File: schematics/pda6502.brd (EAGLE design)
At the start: 100 x 80 mm, 35 parts, among them IC1 74HC00D, IC2 74HC138D, IC3 DS1813-SMD, J1 CON_HEADER_2X07-PTH, U1 W65C02S, U2 W65C22S, U3 28C256, U4 UM61256AK-12

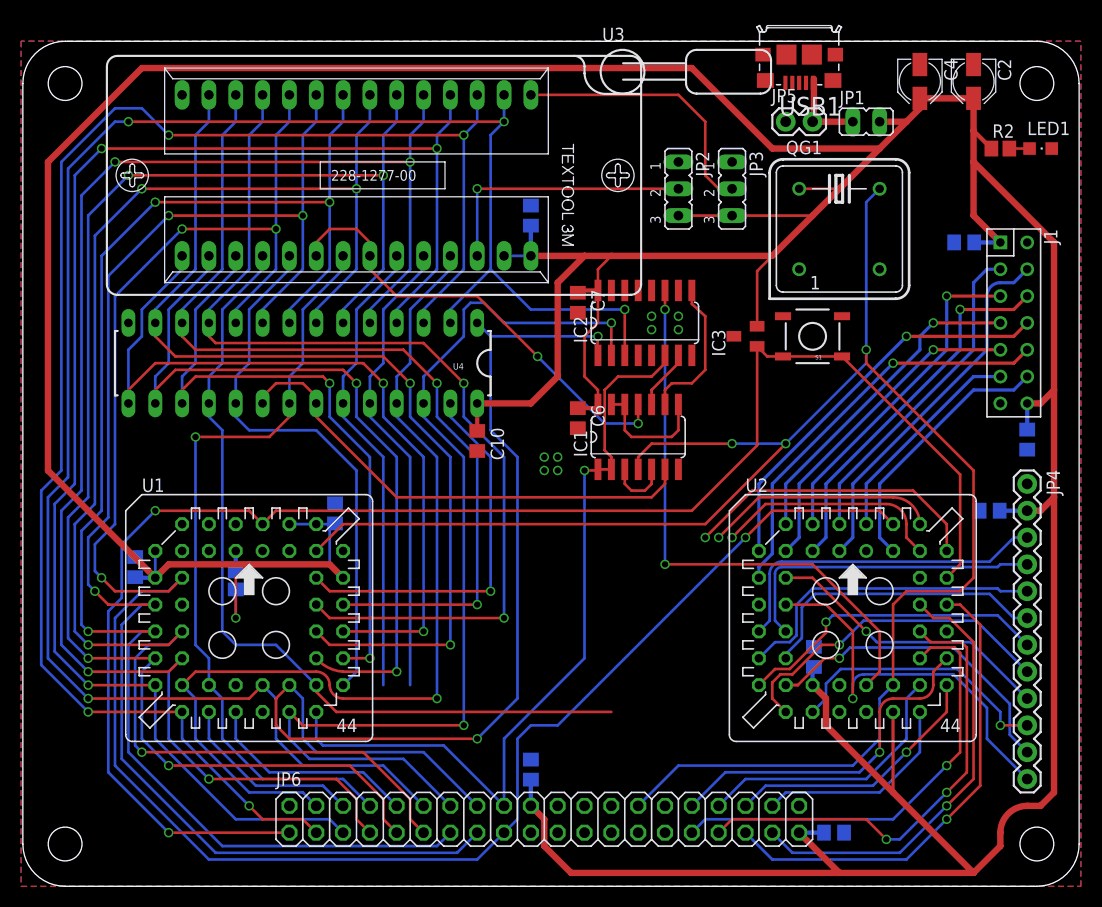
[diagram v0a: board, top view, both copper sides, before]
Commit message: board: 6502 bumped 50 mils right; left-side traces straightened.
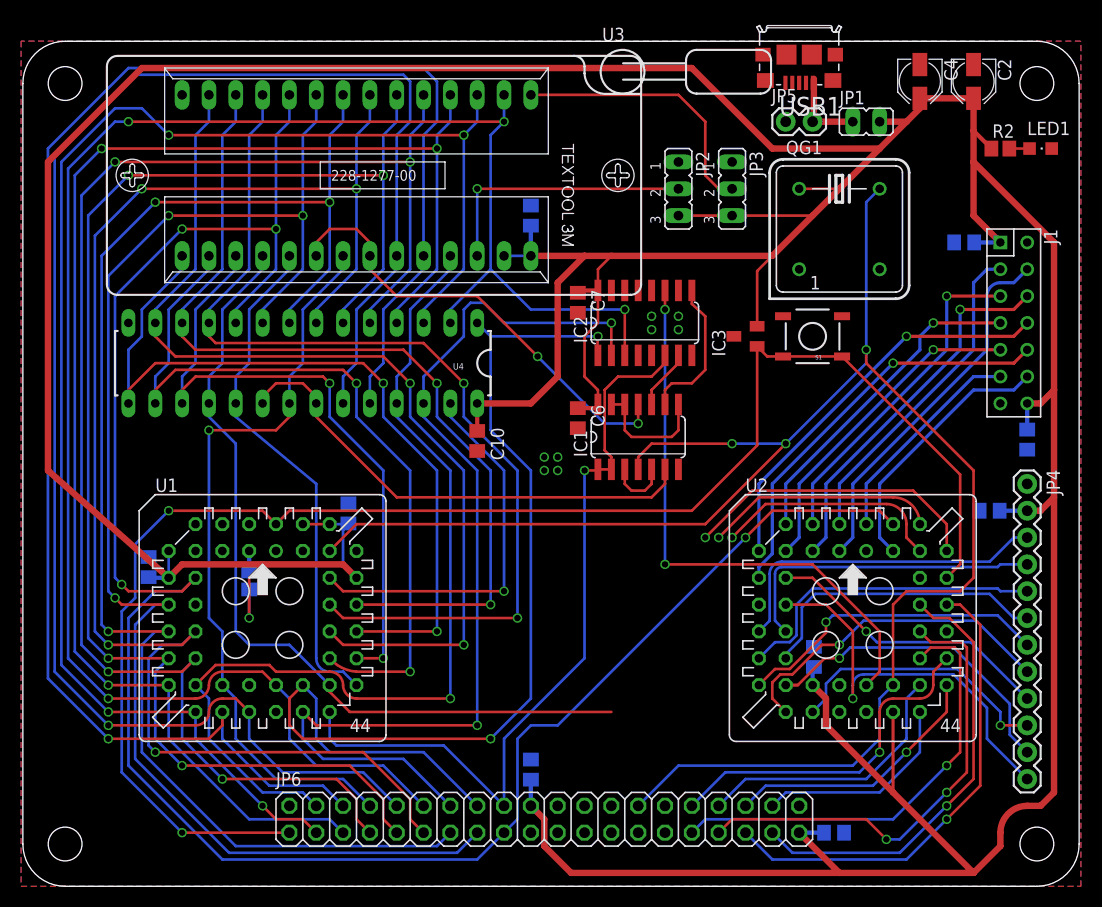
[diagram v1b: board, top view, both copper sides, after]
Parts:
- moved C1 1.27 mm to (12.1, 30.2)
- moved C3 1.27 mm to (31.0, 35.3)
- moved R1 1.27 mm to (21.6, 29.0)
- moved U1 1.27 mm to (22.9, 26.7)
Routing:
- net ADDR9: track 62.2 -> 161.1 mm, vias 0 -> 1
- net ADDR11: track 64.7 -> 160.3 mm, vias 0 -> 1
- net DATA7: track 71.6 -> 68.5 mm
- net ADDR7: track 147.5 -> 144.8 mm
- net ADDR5: track 144.5 -> 141.8 mm
- net ADDR4: track 140.1 -> 137.4 mm
- net ADDR3: track 173.9 -> 171.2 mm
- net ADDR2: track 159.9 -> 157.3 mm
- net ADDR6: track 142.3 -> 139.6 mm
- net RESB: track 150.6 -> 148.1 mm
- net ADDR1: track 158.1 -> 155.8 mm
- net ADDR0: track 195.9 -> 193.5 mm
- net ADDR10: track 73.3 -> 71.1 mm
- net ADDR12: track 177.2 -> 175.6 mm
- net PHI2: track 165.3 -> 164.1 mm
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
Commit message: board: 6502 bumped further right; opens gap for ground pour.
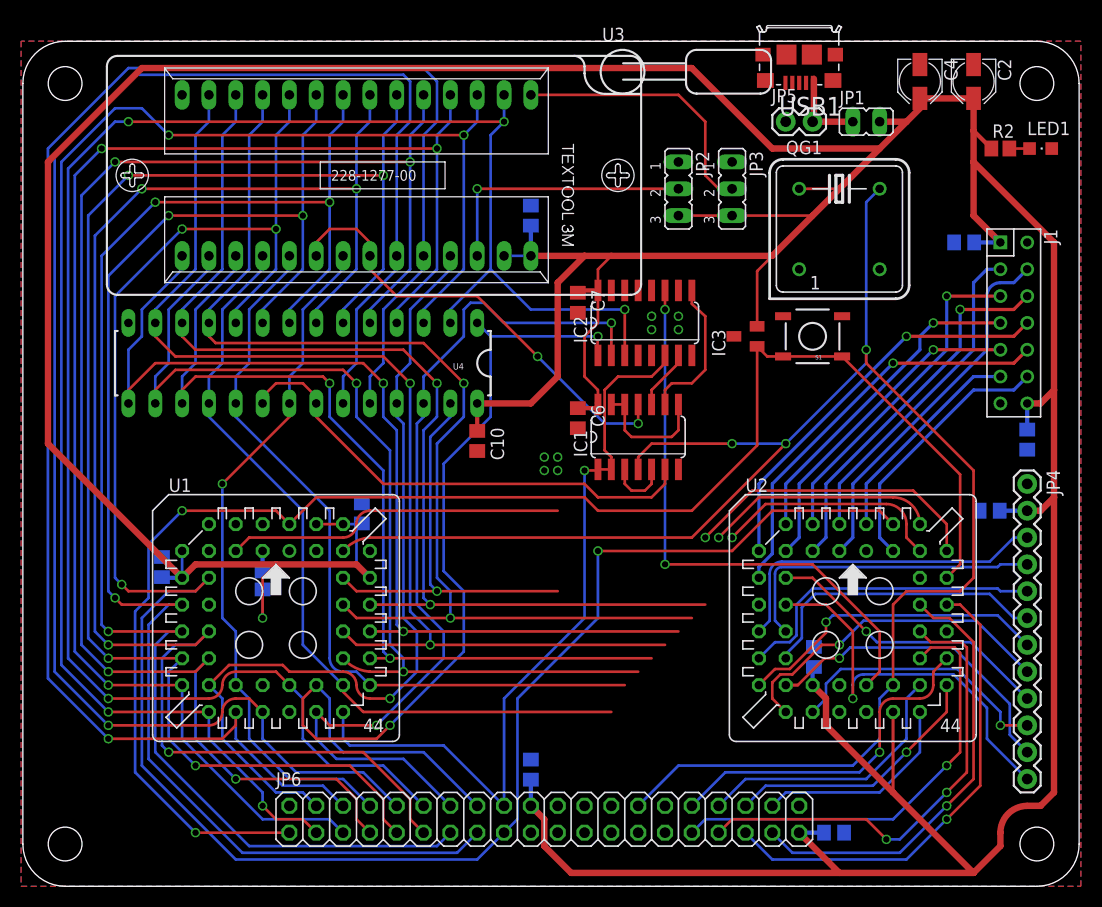
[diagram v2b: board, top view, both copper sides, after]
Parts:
- moved C3 1.27 mm to (32.3, 35.3)
- moved C1 1.27 mm to (13.3, 30.2)
- moved R1 1.27 mm to (22.9, 29.0)
- moved U1 1.27 mm to (24.1, 26.7)
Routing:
- net IRQB: track 0.00 -> 32.1 mm
- net DATA5: track 88.8 -> 113.2 mm
- net DATA7: track 68.5 -> 92.8 mm
- net DATA3: track 118.9 -> 139.2 mm
- net DATA4: track 107.9 -> 128.0 mm
- net DATA1: track 132.1 -> 149.8 mm
- net DATA2: track 135.4 -> 151.8 mm
- net DATA0: track 135.8 -> 150.5 mm
- net ADDR14: track 102.7 -> 92.2 mm
- net ADDR13: track 97.3 -> 87.1 mm
- net ADDR8: track 90.7 -> 82.2 mm
- net ADDR0: track 193.5 -> 199.5 mm
- net ADDR10: track 71.1 -> 65.6 mm
- net DATA6: track 103.1 -> 100.1 mm
- net RWB: track 36.9 -> 39.7 mm
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
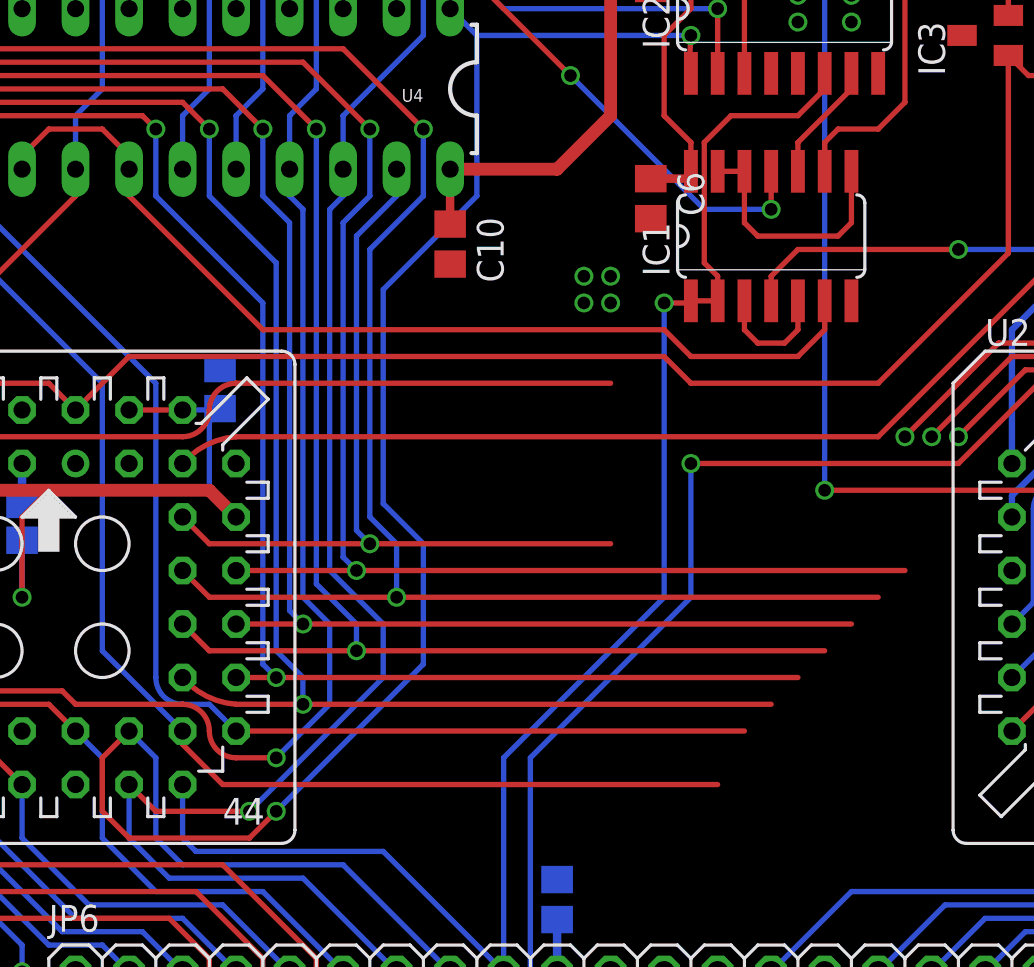
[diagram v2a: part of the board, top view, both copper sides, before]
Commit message: board: clearance to right of 6502 for ground pour.
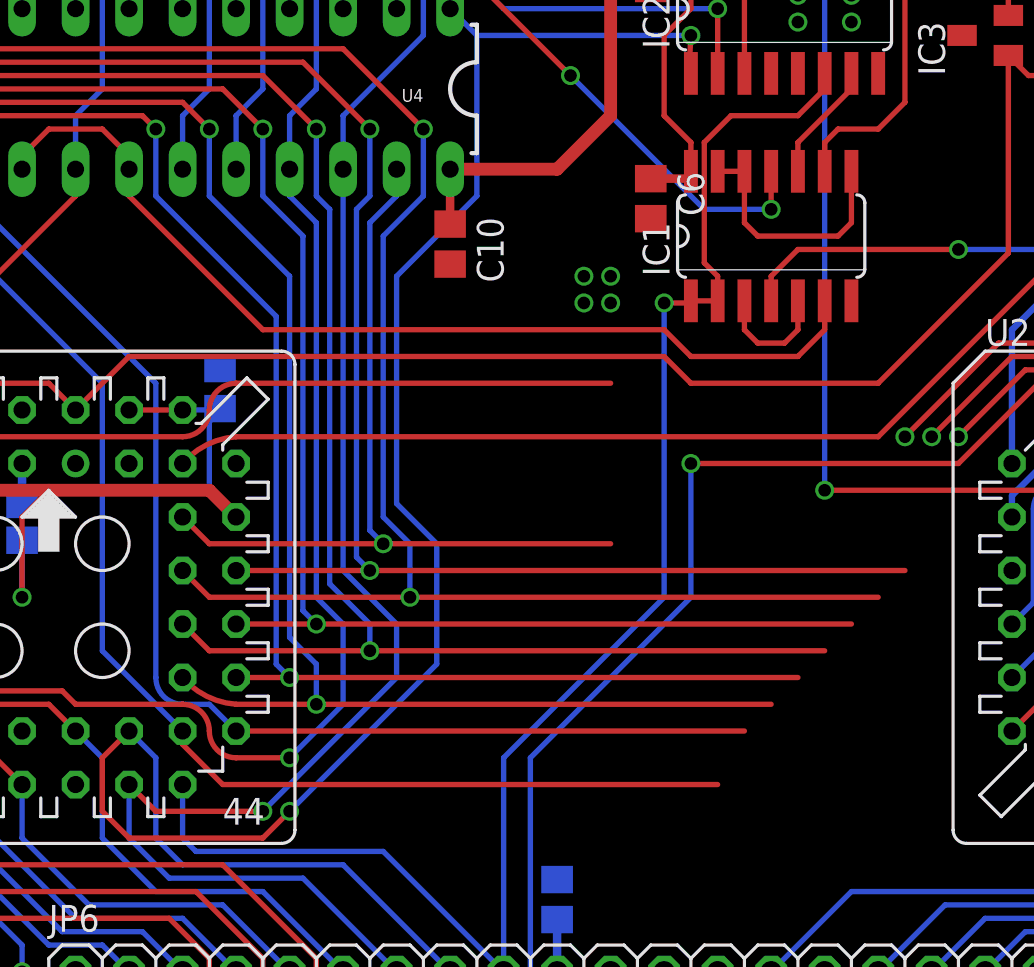
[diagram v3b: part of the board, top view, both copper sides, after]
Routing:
- net ADDR8: track 82.2 -> 83.1 mm

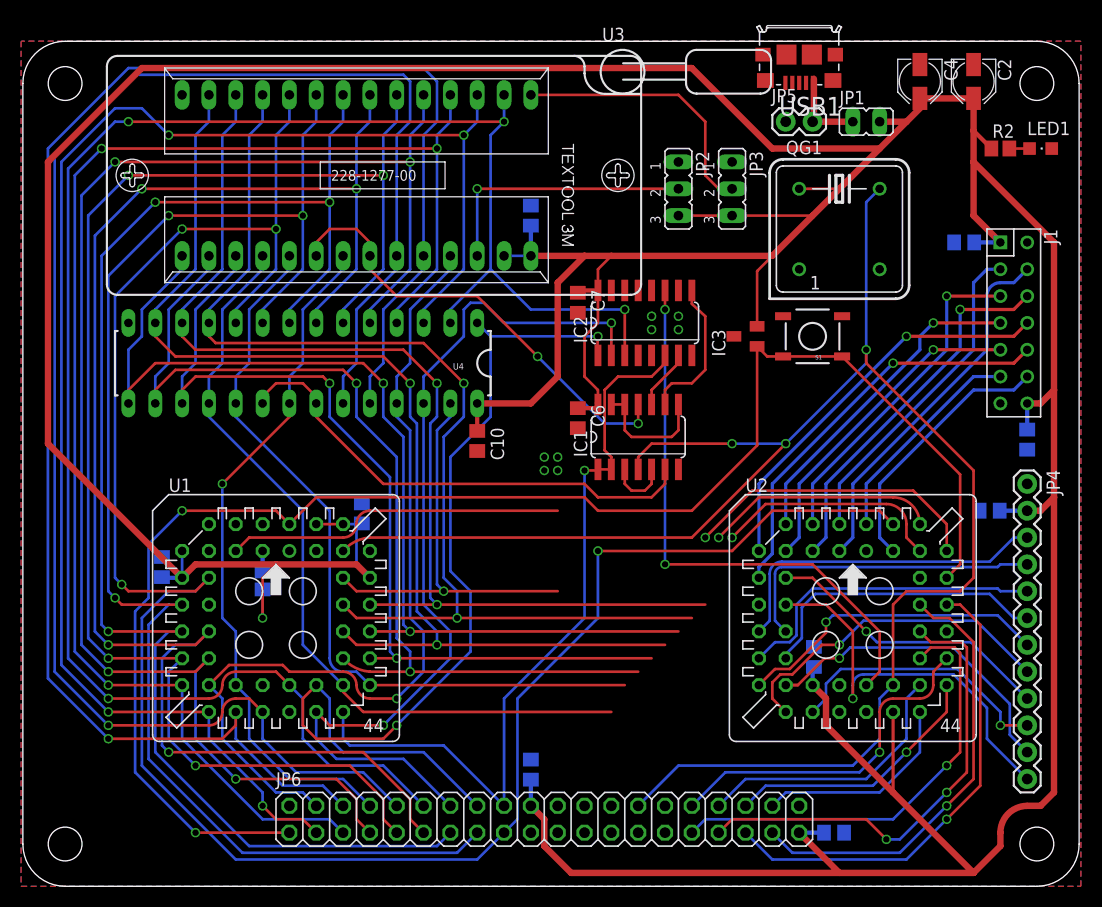
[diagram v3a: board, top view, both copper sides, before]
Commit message: board: 6 airwires; likely all GND plane issues.
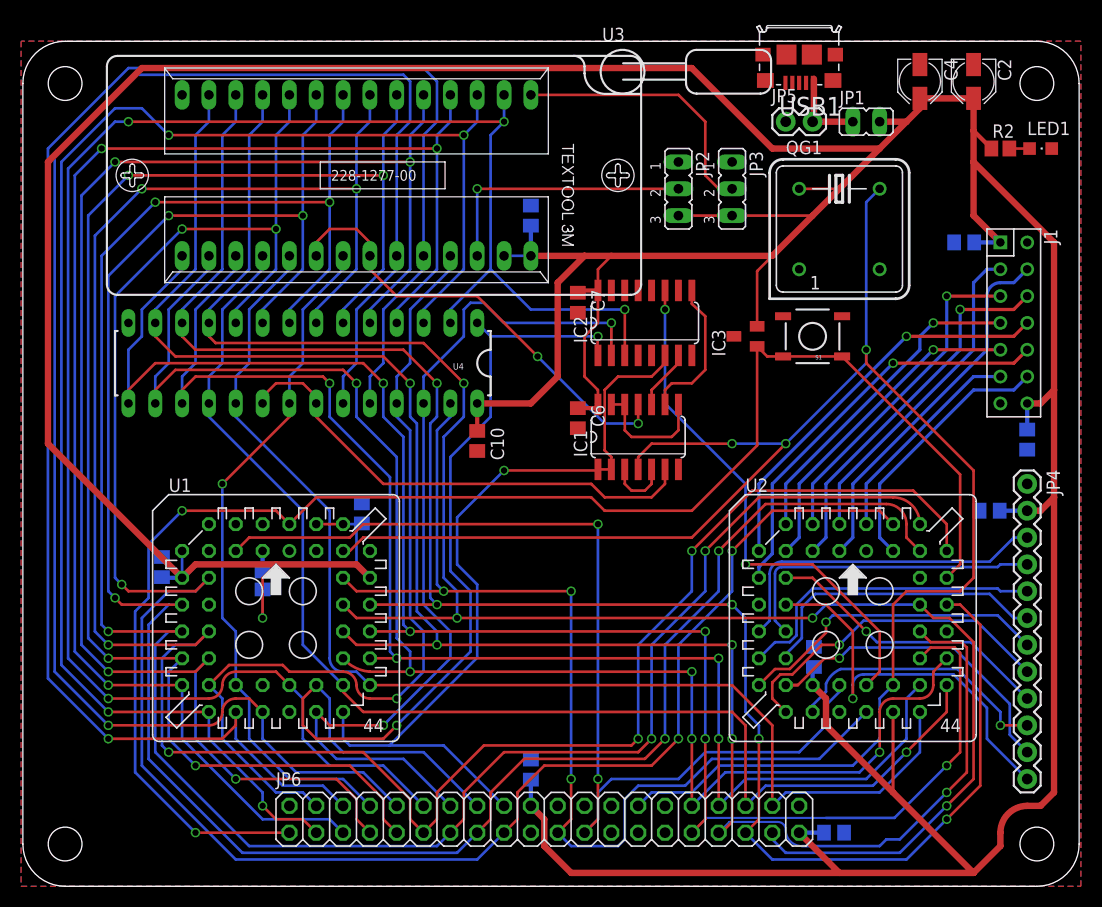
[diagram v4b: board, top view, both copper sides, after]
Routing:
- net IRQB: track 32.1 -> 98.0 mm, vias 0 -> 2
- net RWB: track 39.4 -> 101.3 mm, vias 1 -> 3
- net ADDR3: track 171.2 -> 218.4 mm, vias 5 -> 6
- net ADDR2: track 157.3 -> 203.2 mm, vias 4 -> 5
- net ADDR1: track 155.8 -> 200.4 mm, vias 4 -> 5
- net DATA1: track 149.5 -> 175.2 mm, vias 3 -> 5
- net DATA2: track 152.1 -> 177.2 mm, vias 4 -> 5
- net DATA7: track 92.8 -> 115.9 mm
- net DATA0: track 150.3 -> 172.7 mm, vias 3 -> 4
- net DATA3: track 139.5 -> 161.6 mm, vias 3 -> 5
- net DATA6: track 100.1 -> 120.9 mm
- net DATA5: track 113.5 -> 133.8 mm, vias 2 -> 4
- net DATA4: track 128.3 -> 146.0 mm, vias 3 -> 5
- net ADDR15: track 73.2 -> 78.0 mm
- net VIA_CE: track 54.5 -> 50.0 mm
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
